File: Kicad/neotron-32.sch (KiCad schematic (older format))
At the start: 14 parts, among them J101 Conn_02x06, J102 Conn_02x06, J103 Conn_02x04, U101 EK-TM4C123GXL

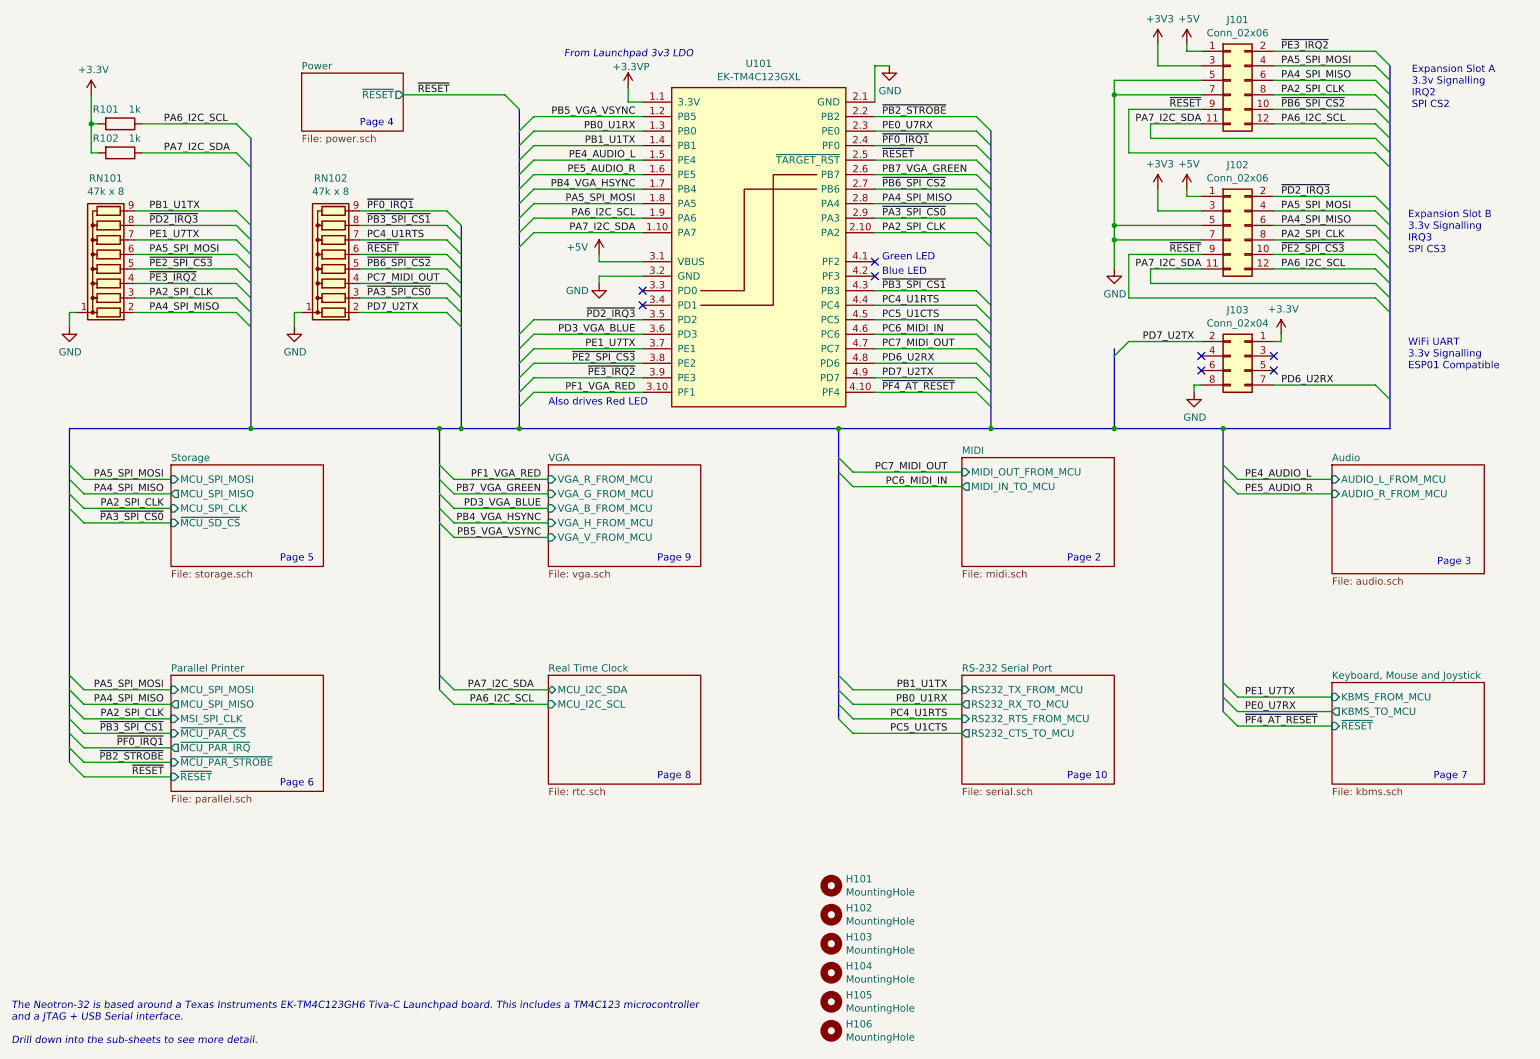
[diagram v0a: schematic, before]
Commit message: Switch to 1598D enclosure.
Use MIC2005A current limiter on input.
Use soft on/off switch from Atmega.
Atmega connects to Tiva over I2C.
Use full-size SD card.
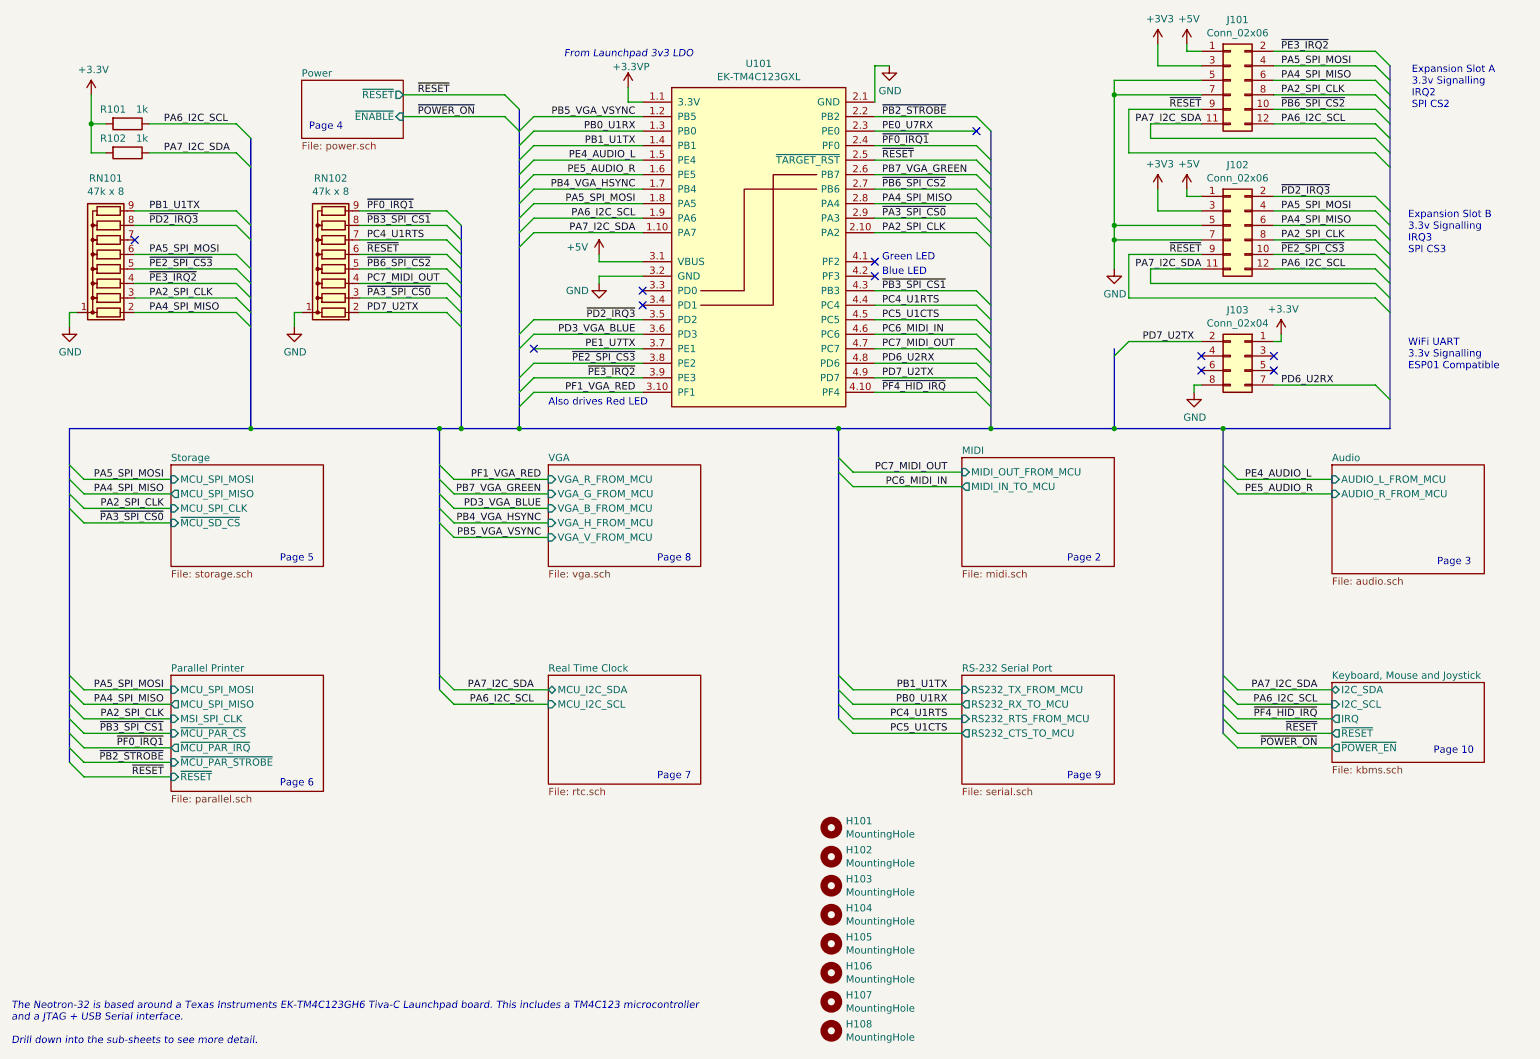
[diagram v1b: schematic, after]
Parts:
- added H107, H108: MountingHole, MountingHole:MountingHole_3.5mm_Pad_Via, symbol Mechanical:MountingHole
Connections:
- net PE1_U7TX: no longer RN101.7 (R6)
- net ~PF4_AT_RESET renamed ~PF4_HID_IRQ
- no-connect marks 8 -> 11
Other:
- moved on the sheet: H101, H102, H103, H104, H105, H106, R101, R102

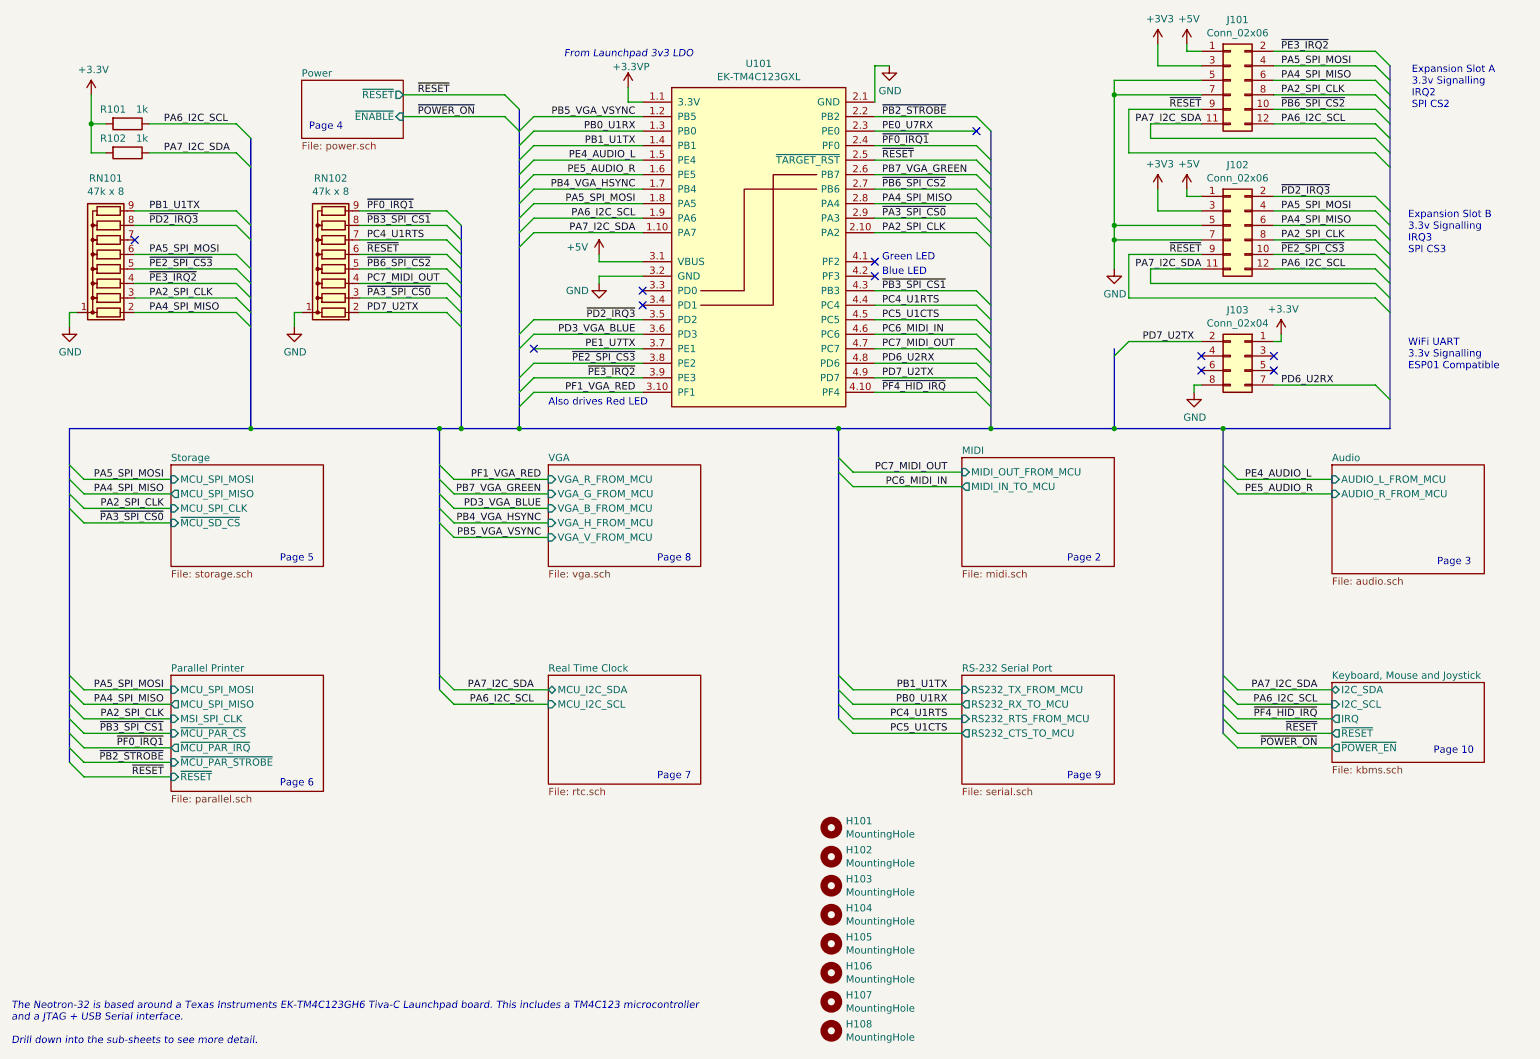
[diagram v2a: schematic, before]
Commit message: Moved Joystick controller onto its own sheet.
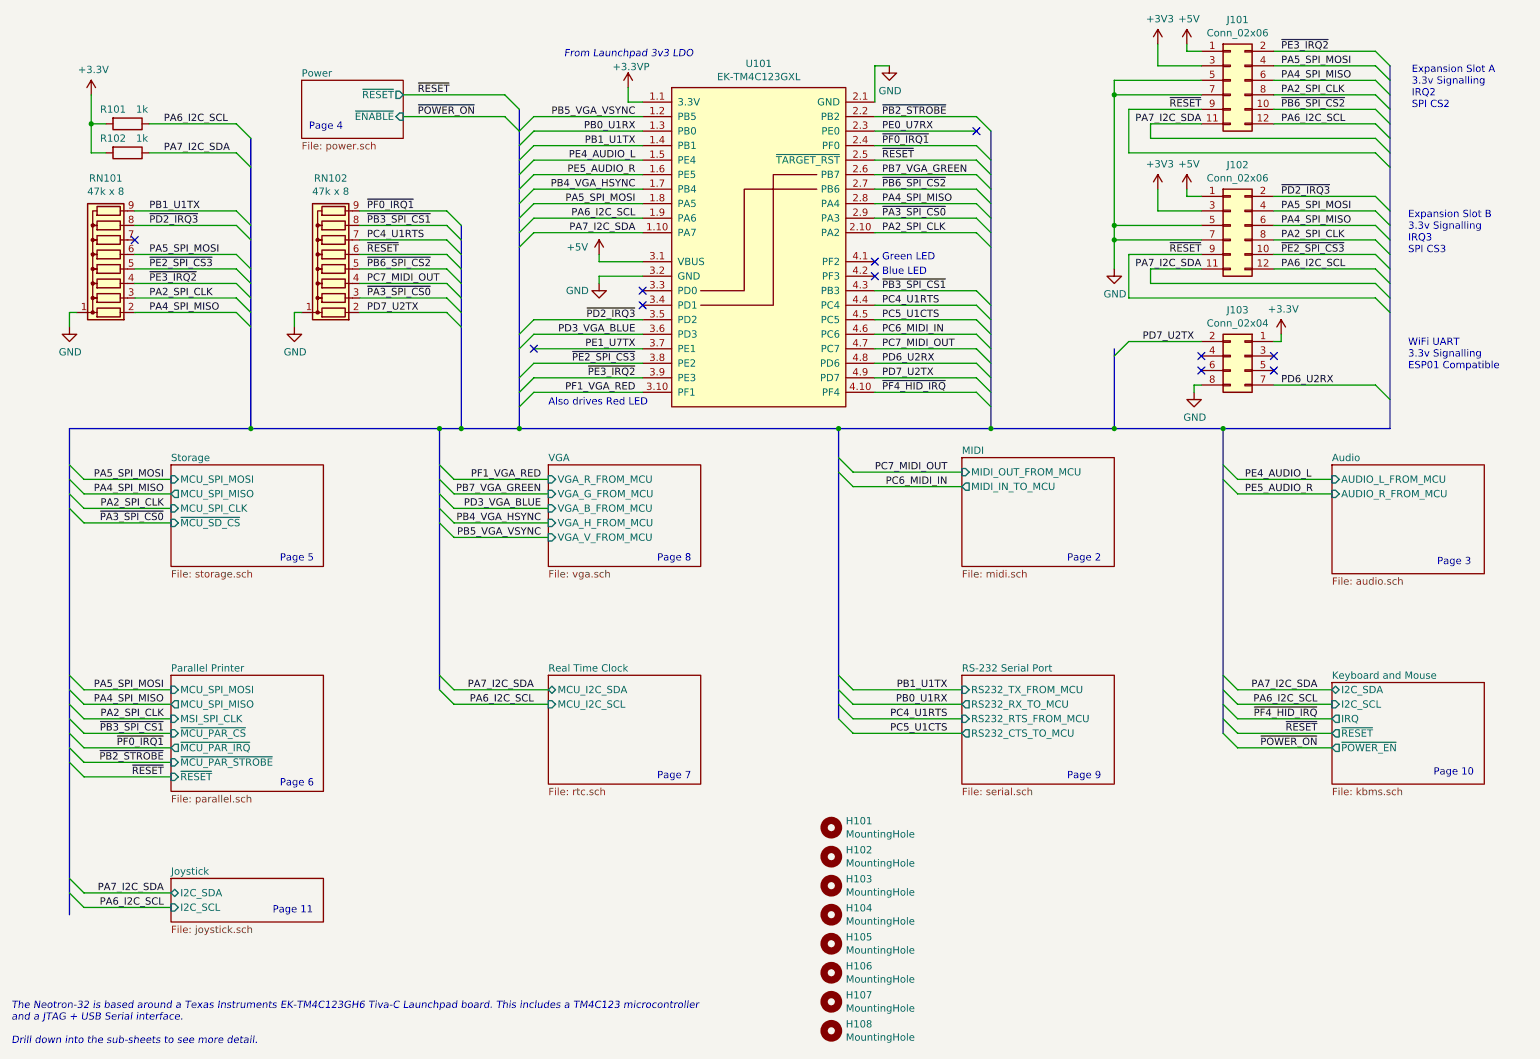
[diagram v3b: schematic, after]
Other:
- note added: "Page 11"
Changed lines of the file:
@@
 $Descr A4 11693 8268
 encoding utf-8
-Sheet 1 12
+Sheet 1 13
 Title "Neotron 32K Main PCB"
 Date "2020-03-29"
@@
 Text Notes 10375 4400 0    50   ~ 0
 Page 3
-Text Notes 10350 5700 0    50   ~ 0
+Text Notes 10350 5850 0    50   ~ 0
 Page 10
 Text Notes 10175 2250 0    50   ~ 0
@@
 Also drives Red LED
 $Sheet
-S 9650 5200 1050 550
+S 9650 5200 1050 700
 U 5DF2662E
-F0 "Keyboard, Mouse and Joystick" 50
+F0 "Keyboard and Mouse" 50
 F1 "kbms.sch" 50
 F2 "I2C_SCL" I L 9650 5350 50
@@
 	1    0    0    -1
 $EndComp
+$Sheet
+S 1650 6550 1050 300
+U 5F46EF57
+F0 "Joystick" 50
+F1 "joystick.sch" 50
+F2 "I2C_SCL" I L 1650 6750 50
+F3 "I2C_SDA" B L 1650 6650 50
+$EndSheet
+Wire Wire Line
+	1050 6750 1650 6750
+Wire Wire Line
+	1050 6650 1650 6650
+Text Label 1600 6650 2    50   ~ 0
+PA7_I2C_SDA
+Text Label 1600 6750 2    50   ~ 0
+PA6_I2C_SCL
+Entry Wire Line
+	1050 6750 950  6650
+Entry Wire Line
+	1050 6650 950  6550
 Wire Bus Line
 	8150 2900 8150 3450
@@
 	3650 2050 3650 3450
 Wire Bus Line
-	950  3450 950  5750
-Wire Bus Line
 	4050 1250 4050 3450
 Wire Bus Line
 	7300 1400 7300 3450
 Wire Bus Line
+	950  3450 950  6800
+Wire Bus Line
 	10050 950  10050 3450
+Text Notes 2350 6800 0    50   ~ 0
+Page 11
 $EndSCHEMATC
